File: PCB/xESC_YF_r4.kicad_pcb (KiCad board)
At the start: 2 copper layers, 49.5 x 29 mm, 50 parts, among them J1 Conn_01x09_Male, J10 OM-MB W => MC BRK, J2 Conn_01x03_Pin, J3 Conn_01x05_Male, J4 Conn_01x05_Male, J6 OM-MB U <= MC SA, J7 Conn_01x06_Male, J8 Conn_01x06_Pin, J9 OM-MB V => MC +24V, Q1 2N7002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

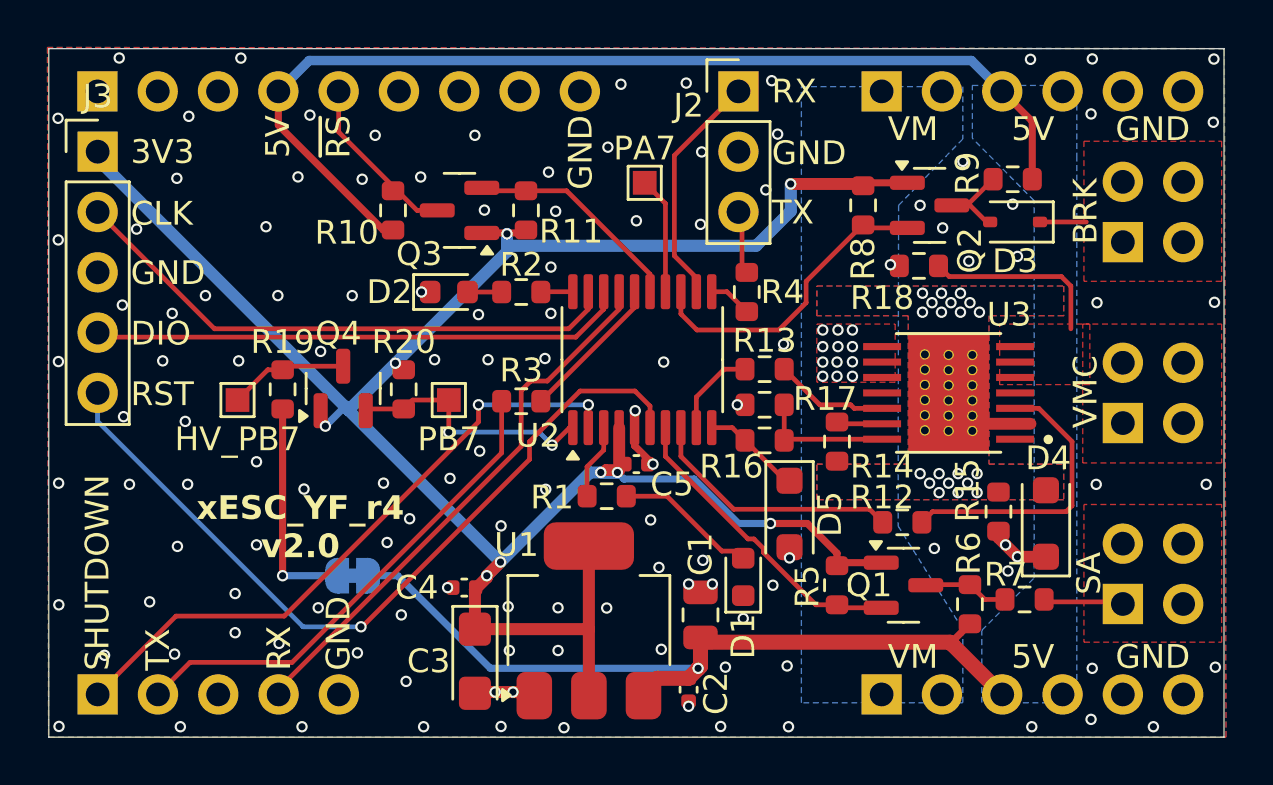
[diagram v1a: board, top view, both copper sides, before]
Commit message: Fix ERC/DRC
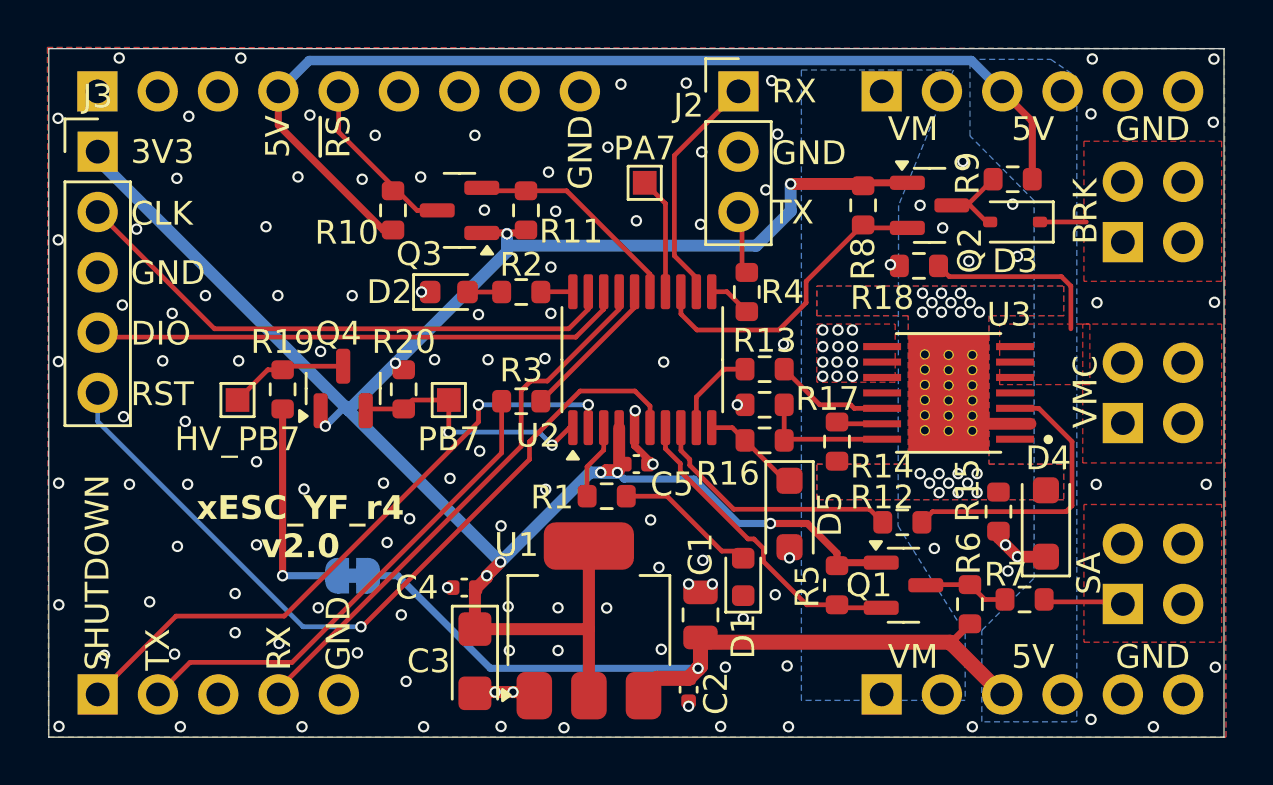
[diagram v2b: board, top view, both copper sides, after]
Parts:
- R1, R2, R3, R4, R7: value 220 -> 220
- R8, R9: value 470 -> 470
- turned R16 to 0 degrees
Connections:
- R16 pad 1: Net-(U3-CS) -> /CUR_SENSE
- R16 pad 2: /CUR_SENSE -> Net-(U3-CS)
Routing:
- net GND: vias 126 -> 124
